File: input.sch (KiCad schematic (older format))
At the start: 64 parts, among them U301 NE5532, U302 NE5532, U303 NE5532, U304 NE5532

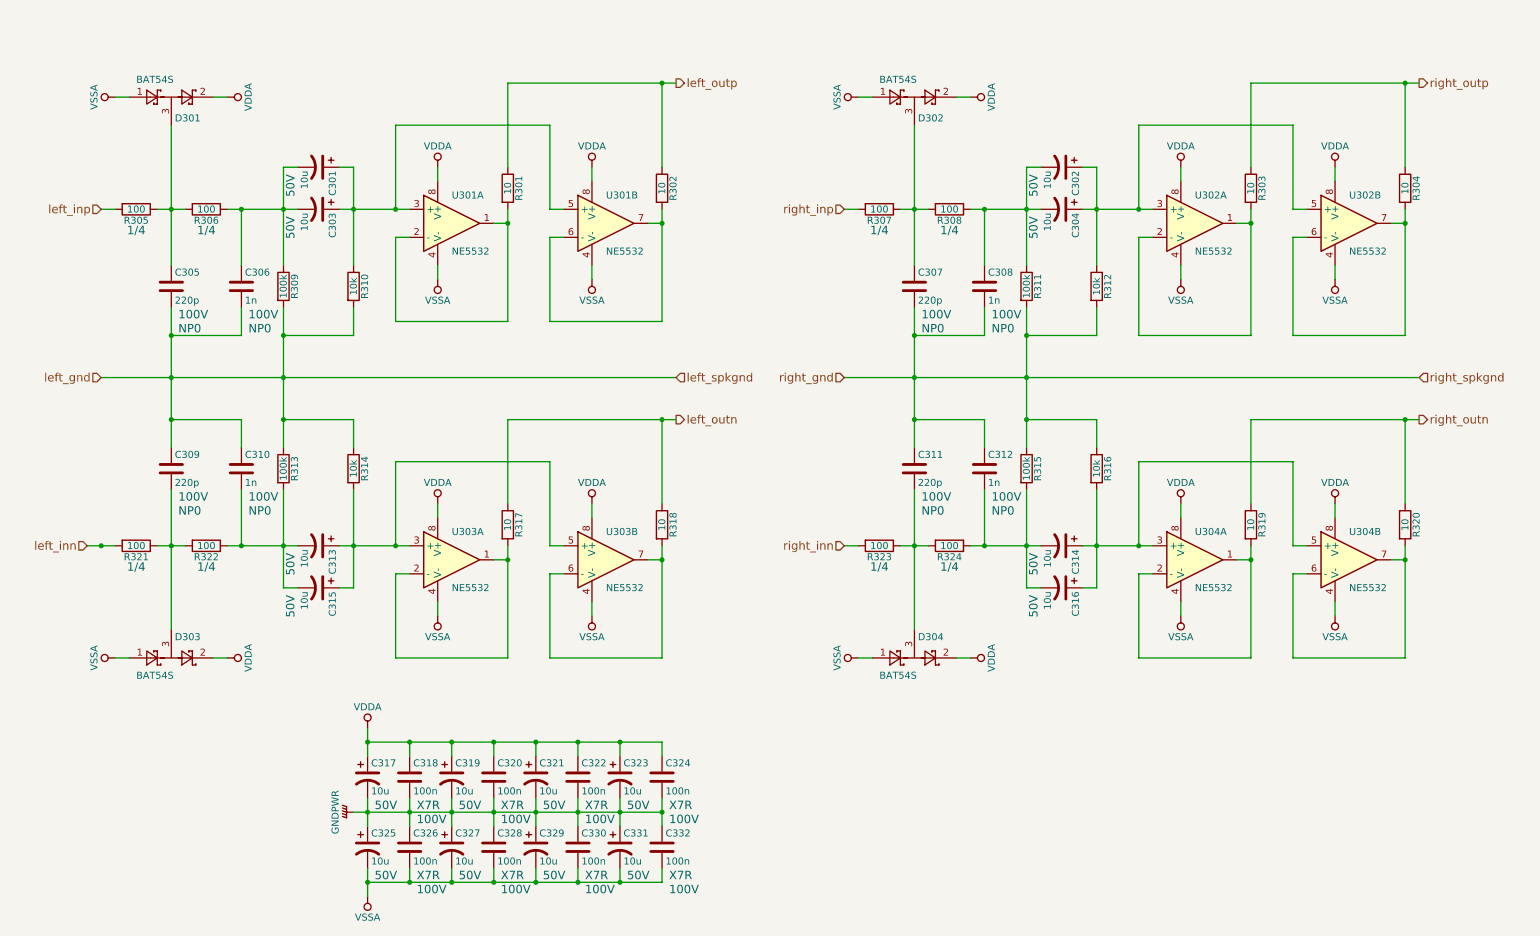
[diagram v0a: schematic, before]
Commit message: The board shall now support single channel only.
Signed-off-by: Nenad Radulovic <nenad.radulovic@seavus.com>
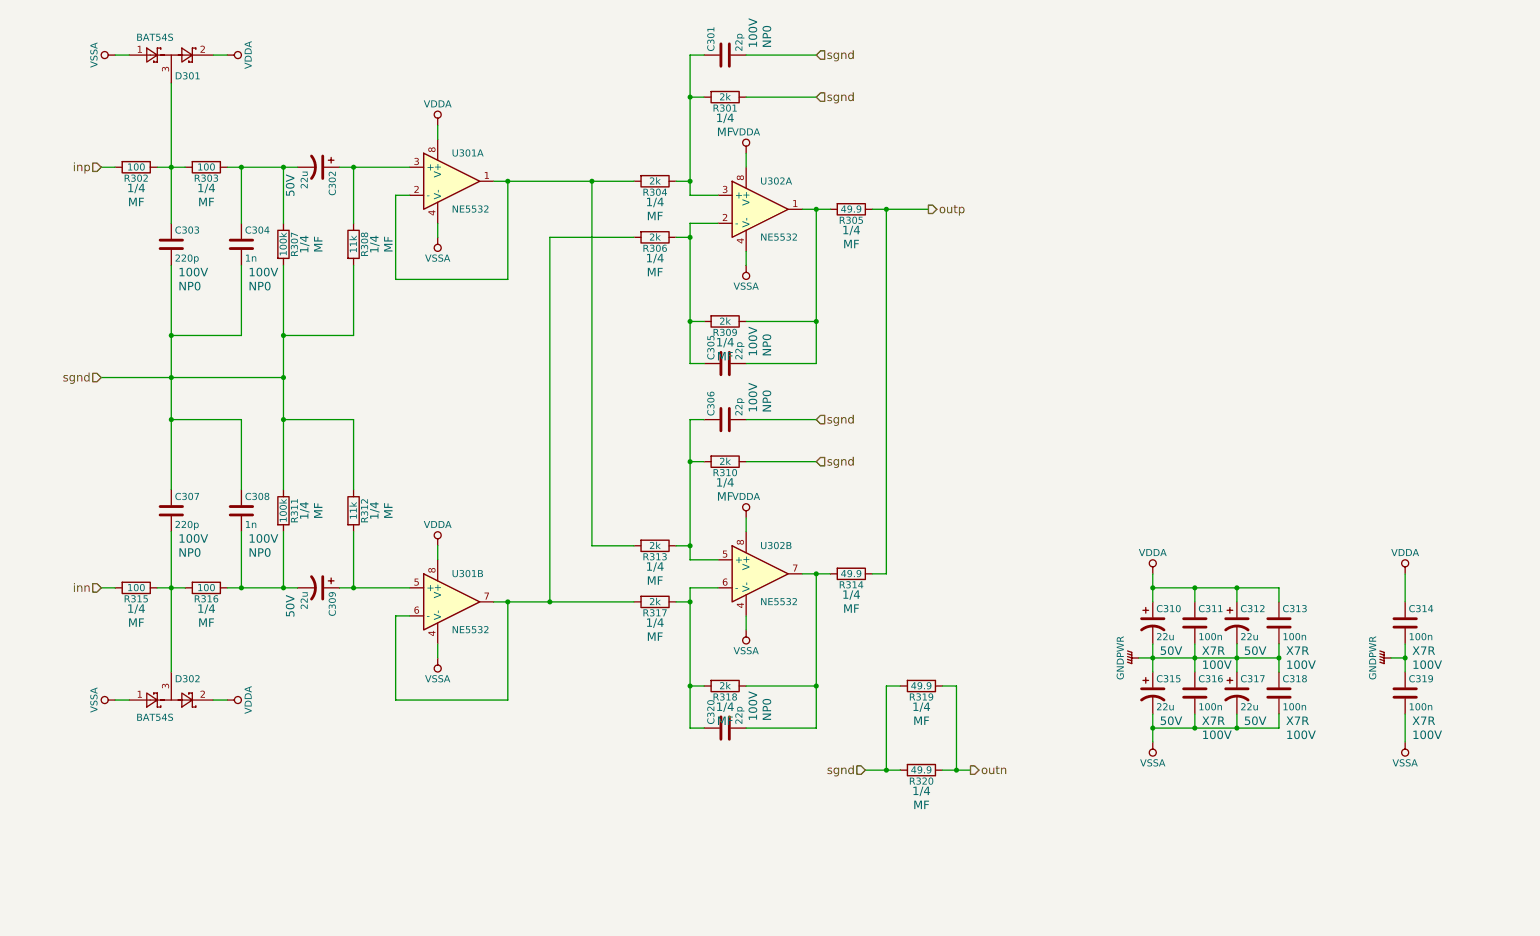
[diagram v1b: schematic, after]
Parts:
- removed C301, C302, C304, C314, C315, C316, C321, C323, C329, C331: 10u, Capacitor_THT:CP_Radial_D5.0mm_P2.00mm, symbol CP1
- removed C307, C311: 220p, Capacitor_SMD:C_0805_2012Metric_Pad1.15x1.50mm_HandSolder, symbol C
- removed C308, C312: 1n, Capacitor_SMD:C_0805_2012Metric_Pad1.15x1.50mm_HandSolder, symbol C
- removed C322, C324, C330, C332: 100n, Capacitor_SMD:C_1206_3216Metric_Pad1.24x1.80mm_HandSolder, symbol C
- removed D302, D304: BAT54S, Package_TO_SOT_SMD:SOT-23_Handsoldering, symbol BAT54S
- removed R321, R322, R323, R324: 100, Resistor_SMD:R_1206_3216Metric, symbol R
- removed unit 1 of U302
- removed unit 2 of U303
- removed U304: NE5532, Housings_DIP:DIP-8_W7.62mm_LongPads, symbol NE5532
- added C301, C305, C306, C320: 22p, Capacitor_SMD:C_0805_2012Metric_Pad1.15x1.50mm_HandSolder, symbol C
- added C314, C319: 100n, Capacitor_SMD:C_1206_3216Metric_Pad1.24x1.80mm_HandSolder, symbol C
- C302: renamed from C303; value 10u -> 22u; Manufacturer Rybicon:50YXF10MEFC5X11 -> Rybicon:50YXJ22MTA5X11; Vendor Farnell:1144632 -> Farnell:2346268
- C309: renamed from C313; value 10u -> 22u; Manufacturer Rybicon:50YXF10MEFC5X11 -> Rybicon:50YXJ22MTA5X11; Vendor Farnell:1144632 -> Farnell:2346268
- C310: renamed from C317; value 10u -> 22u; Manufacturer Rybicon:50YXF10MEFC5X11 -> Rybicon:50YXJ22MTA5X11; Vendor Farnell:1144632 -> Farnell:2346268
- C312: renamed from C319; value 10u -> 22u; Manufacturer Rybicon:50YXF10MEFC5X11 -> Rybicon:50YXJ22MTA5X11; Vendor Farnell:1144632 -> Farnell:2346268
- C315: renamed from C325; value 10u -> 22u; Manufacturer Rybicon:50YXF10MEFC5X11 -> Rybicon:50YXJ22MTA5X11; Vendor Farnell:1144632 -> Farnell:2346268
- C317: renamed from C327; value 10u -> 22u; Manufacturer Rybicon:50YXF10MEFC5X11 -> Rybicon:50YXJ22MTA5X11; Vendor Farnell:1144632 -> Farnell:2346268
- R301, R304, R317, R318: value 10 -> 2k; footprint Resistor_SMD:R_1206_3216Metric -> Resistor_SMD:R_1206_3216Metric_Pad1.24x1.80mm_HandSolder; Manufacturer (none) -> PANASONIC:ERA8ARB202V; Power (none) -> 1/4; Type (none) -> MF; Vendor (none) -> Farnell:2484813
- R302, R303: value 10 -> 100; footprint Resistor_SMD:R_1206_3216Metric -> Resistor_SMD:R_1206_3216Metric_Pad1.24x1.80mm_HandSolder; Manufacturer (none) -> PANASONIC:ERA8AEB101V; Power (none) -> 1/4; Type (none) -> MF; Vendor (none) -> Farnell:1717738
- R305: value 100 -> 49.9; footprint Resistor_SMD:R_1206_3216Metric -> Resistor_SMD:R_1206_3216Metric_Pad1.24x1.80mm_HandSolder; Manufacturer (none) -> PANASONIC:ERA8AEB49R9V; Type (none) -> MF; Vendor (none) -> Farnell:2095158
- R306: value 100 -> 2k; footprint Resistor_SMD:R_1206_3216Metric -> Resistor_SMD:R_1206_3216Metric_Pad1.24x1.80mm_HandSolder; Manufacturer (none) -> PANASONIC:ERA8ARB202V; Type (none) -> MF; Vendor (none) -> Farnell:2484813
- R307: value 100 -> 100k; footprint Resistor_SMD:R_1206_3216Metric -> Resistor_SMD:R_1206_3216Metric_Pad1.24x1.80mm_HandSolder; Manufacturer (none) -> PANASONIC:ERA8AEB104V; Type (none) -> MF; Vendor (none) -> Farnell:1717758
- R308: value 100 -> 11k; footprint Resistor_SMD:R_1206_3216Metric -> Resistor_SMD:R_1206_3216Metric_Pad1.24x1.80mm_HandSolder; Manufacturer (none) -> PANASONIC:ERA8ARB113V; Type (none) -> MF; Vendor (none) -> Farnell:2484802
- R309, R313: value 100k -> 2k; footprint Resistor_SMD:R_1206_3216Metric -> Resistor_SMD:R_1206_3216Metric_Pad1.24x1.80mm_HandSolder; Manufacturer (none) -> PANASONIC:ERA8ARB202V; Power (none) -> 1/4; Type (none) -> MF; Vendor (none) -> Farnell:2484813
- R310: value 10k -> 2k; footprint Resistor_SMD:R_1206_3216Metric -> Resistor_SMD:R_1206_3216Metric_Pad1.24x1.80mm_HandSolder; Manufacturer (none) -> PANASONIC:ERA8ARB202V; Power (none) -> 1/4; Type (none) -> MF; Vendor (none) -> Farnell:2484813
- R311: footprint Resistor_SMD:R_1206_3216Metric -> Resistor_SMD:R_1206_3216Metric_Pad1.24x1.80mm_HandSolder; Manufacturer (none) -> PANASONIC:ERA8AEB104V; Power (none) -> 1/4; Type (none) -> MF; Vendor (none) -> Farnell:1717758
- R312: value 10k -> 11k; footprint Resistor_SMD:R_1206_3216Metric -> Resistor_SMD:R_1206_3216Metric_Pad1.24x1.80mm_HandSolder; Manufacturer (none) -> PANASONIC:ERA8ARB113V; Power (none) -> 1/4; Type (none) -> MF; Vendor (none) -> Farnell:2484802
- R314: value 10k -> 49.9; footprint Resistor_SMD:R_1206_3216Metric -> Resistor_SMD:R_1206_3216Metric_Pad1.24x1.80mm_HandSolder; Manufacturer (none) -> PANASONIC:ERA8AEB49R9V; Power (none) -> 1/4; Type (none) -> MF; Vendor (none) -> Farnell:2095158
- R315: value 100k -> 100; footprint Resistor_SMD:R_1206_3216Metric -> Resistor_SMD:R_1206_3216Metric_Pad1.24x1.80mm_HandSolder; Manufacturer (none) -> PANASONIC:ERA8AEB101V; Power (none) -> 1/4; Type (none) -> MF; Vendor (none) -> Farnell:1717738
- R316: value 10k -> 100; footprint Resistor_SMD:R_1206_3216Metric -> Resistor_SMD:R_1206_3216Metric_Pad1.24x1.80mm_HandSolder; Manufacturer (none) -> PANASONIC:ERA8AEB101V; Power (none) -> 1/4; Type (none) -> MF; Vendor (none) -> Farnell:1717738
- R319, R320: value 10 -> 49.9; footprint Resistor_SMD:R_1206_3216Metric -> Resistor_SMD:R_1206_3216Metric_Pad1.24x1.80mm_HandSolder; Manufacturer (none) -> PANASONIC:ERA8AEB49R9V; Power (none) -> 1/4; Type (none) -> MF; Vendor (none) -> Farnell:2095158
- renumbered C305 to C303, C306 to C304, C309 to C307, C310 to C308, C318 to C311, C320 to C313, C326 to C316, C328 to C318, D303 to D302, U303 to U301, U301 to U302
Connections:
- net right_inp is gone; now on net sgnd: R307.2
- net GNDPWR: now also C314.2, C319.1
- net VDDA: now also C314.1
- net VSSA: now also C319.2
- net at U301.1, U301.2 (-): now also R304.2, R313.2; no longer R301.2
- net at C302.1, U301.3 (+): now also R308.1; no longer R310.1, U302.5 (+)
- net at C302.2, C304.1: now also R303.1, R307.1; no longer R306.1, R309.1
- net at C303.1, D301.3: now also R302.1, R303.2; no longer R305.1, R306.2
- net at R318.2: now also R317.1, U302.6 (-), C320.1
- net at C308.2, C309.2: now also R311.2, R316.1; no longer R313.2
- net at C307.2, D302.3: now also R315.1, R316.2
- net at U302.5 (+): now also R310.2, R313.1, C306.1; no longer R312.1
- net sgnd: now reaches R311.1
- net sgnd: now also C303.2, C304.2, C307.1, C308.1, R301.1, R308.2, R310.1, R312.1, R319.2, R320.2, C301.2, C306.2; no longer R308.1
- net inn: now reaches R315.2
- removed net left_gnd: C303.2, C304.2, C307.1, C308.1, R309.2, R310.2, R313.1, R314.1
- net left_inp: no longer names the net of R305.2
- net left_inp: now also R309.1, U302.1, C305.2
- net left_outn: no longer names the net of R318.1
- net left_outn: now also R314.2, U302.7, C320.2; no longer R317.1
- removed net left_outp: R301.1, R302.1
- removed net right_gnd: R311.2, R312.2, R315.1, R316.1
- net right_outn renamed outn
- net right_outp: no longer names the net of R304.1
- net right_outp: now also R301.2, U302.3 (+), C301.1; no longer R303.1
- new net: C305.1, R306.1, R309.2, U302.2 (-)
- new net: C309.1, R312.2, U301.5 (+)
- new net: R306.2, R317.2, U301.6 (-), U301.7
- new net inp: R302.2
- new net outp: R305.1, R314.1
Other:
- moved on the sheet: C302, C303, C304, C307, C308, C309, C310, C311, C312, C313, C315, C316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

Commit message: Switched to Kicad 5.0
Signed-off-by: Nenad Radulovic <nenad.b.radulovic@gmail.com>
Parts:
- removed C301, C305, C306, C320: 22p, Capacitor_SMD:C_0805_2012Metric_Pad1.15x1.50mm_HandSolder, symbol C
- removed C302, C309, C310, C312, C315, C317: 22u, Capacitor_THT:CP_Radial_D5.0mm_P2.00mm, symbol CP1
- removed C307: 220p, Capacitor_SMD:C_0805_2012Metric_Pad1.15x1.50mm_HandSolder, symbol C
- removed C308: 1n, Capacitor_SMD:C_0805_2012Metric_Pad1.15x1.50mm_HandSolder, symbol C
- removed C311, C313, C314, C316, C318, C319: 100n, Capacitor_SMD:C_1206_3216Metric_Pad1.24x1.80mm_HandSolder, symbol C
- removed D301, D302: BAT54S, Package_TO_SOT_SMD:SOT-23_Handsoldering, symbol BAT54S
- removed R301, R304, R306, R309, R310, R313, R317, R318: 2k, Resistor_SMD:R_1206_3216Metric_Pad1.24x1.80mm_HandSolder, symbol R
- removed R305, R314, R319, R320: 49.9, Resistor_SMD:R_1206_3216Metric_Pad1.24x1.80mm_HandSolder, symbol R
- removed R308, R312: 11k, Resistor_SMD:R_1206_3216Metric_Pad1.24x1.80mm_HandSolder, symbol R
- removed R311: 100k, Resistor_SMD:R_1206_3216Metric_Pad1.24x1.80mm_HandSolder, symbol R
- removed R315, R316: 100, Resistor_SMD:R_1206_3216Metric_Pad1.24x1.80mm_HandSolder, symbol R
- removed U301, U302: NE5532, Housings_DIP:DIP-8_W7.62mm_LongPads, symbol NE5532
- added R12: 10, Resistor_THT:R_Axial_DIN0309_L9.0mm_D3.2mm_P12.70mm_Horizontal, symbol Device:R
- C12: renamed from C303; footprint Capacitor_SMD:C_0805_2012Metric_Pad1.15x1.50mm_HandSolder -> Capacitor_THT:C_Disc_D4.3mm_W1.9mm_P5.00mm; symbol C -> Device:C
- C13: renamed from C304; footprint Capacitor_SMD:C_0805_2012Metric_Pad1.15x1.50mm_HandSolder -> Capacitor_THT:C_Disc_D4.3mm_W1.9mm_P5.00mm; symbol C -> Device:C
- R10: renamed from R303; footprint Resistor_SMD:R_1206_3216Metric_Pad1.24x1.80mm_HandSolder -> Resistor_THT:R_Axial_DIN0207_L6.3mm_D2.5mm_P10.16mm_Horizontal; symbol R -> Device:R
- R11: renamed from R307; footprint Resistor_SMD:R_1206_3216Metric_Pad1.24x1.80mm_HandSolder -> Resistor_THT:R_Axial_DIN0207_L6.3mm_D2.5mm_P10.16mm_Horizontal; symbol R -> Device:R
- R9: renamed from R302; footprint Resistor_SMD:R_1206_3216Metric_Pad1.24x1.80mm_HandSolder -> Resistor_THT:R_Axial_DIN0207_L6.3mm_D2.5mm_P10.16mm_Horizontal; symbol R -> Device:R
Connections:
- net GNDPWR: now also R12.1
- net outp: now also C13.1, R10.1, R11.1
- net sgnd: now also R12.2
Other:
- moved on the sheet: R11

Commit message: Release Version 1.0
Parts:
- C12: Manufacturer Multicomp:MCMT21N221F101CT -> AVX:SR211A221JAR; Vendor Farnell:1856271 -> Farnell:1100508
- C13: Manufacturer Multicomp:MCMT21N102F101CT -> AVX:SR211A102KAR; Vendor Farnell:1856276 -> Farnell:1100513
- R10, R9: Manufacturer PANASONIC:ERA8AEB101V -> TE Connectivity:LR0204F100R; Power 1/4 -> 0.25W; Vendor Farnell:1717738 -> Farnell:2329854
- R11: Manufacturer PANASONIC:ERA8AEB104V -> TE Connectivity:LR0204F100K; Power 1/4 -> 0.25W; Vendor Farnell:1717758 -> Farnell:2329853
- R12: footprint Resistor_THT:R_Axial_DIN0309_L9.0mm_D3.2mm_P12.70mm_Horizontal -> Resistor_THT:R_Axial_DIN0207_L6.3mm_D2.5mm_P10.16mm_Horizontal; Manufacturer NEOHM-TE:FRN50J10R/S -> TE Connectivity:LR1F10R; Power 1/4 -> 0.6W; Type MO -> MF; Vendor Farnell:1898502 -> Farnell:2329993
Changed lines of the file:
@@
 F 1 "1n" H 2125 2450 50  0000 L CNN
 F 2 "Capacitor_THT:C_Disc_D4.3mm_W1.9mm_P5.00mm" H 2138 2400 50  0001 C CNN
-F 3 "http://www.farnell.com/datasheets/1825496.pdf" H 2100 2550 50  0001 C CNN
+F 3 "http://www.farnell.com/datasheets/2095938.pdf" H 2100 2550 50  0001 C CNN
 F 4 "100V" H 2150 2350 60  0000 L CNN "Voltage"
 F 5 "NP0" H 2150 2250 60  0000 L CNN "Type"
-F 6 "Farnell:1856276" H 2100 2550 60  0001 C CNN "Vendor"
-F 7 "Multicomp:MCMT21N102F101CT" H 2100 2550 60  0001 C CNN "Manufacturer"
+F 6 "Farnell:1100513" H 2100 2550 60  0001 C CNN "Vendor"
+F 7 "AVX:SR211A102KAR" H 2100 2550 60  0001 C CNN "Manufacturer"
 	1    2100 2550
 	1    0    0    -1
@@
 F 1 "220p" H 1625 2450 50  0000 L CNN
 F 2 "Capacitor_THT:C_Disc_D4.3mm_W1.9mm_P5.00mm" H 1638 2400 50  0001 C CNN
-F 3 "http://www.farnell.com/datasheets/1825496.pdf" H 1600 2550 50  0001 C CNN
+F 3 "http://www.farnell.com/datasheets/2095938.pdf" H 1600 2550 50  0001 C CNN
 F 4 "100V" H 1650 2350 60  0000 L CNN "Voltage"
 F 5 "NP0" H 1650 2250 60  0000 L CNN "Type"
-F 6 "Farnell:1856271" H 1600 2550 60  0001 C CNN "Vendor"
-F 7 "Multicomp:MCMT21N221F101CT" H 1600 2550 60  0001 C CNN "Manufacturer"
+F 6 "Farnell:1100508" H 1600 2550 60  0001 C CNN "Vendor"
+F 7 "AVX:SR211A221JAR" H 1600 2550 60  0001 C CNN "Manufacturer"
 	1    1600 2550
 	1    0    0    -1
@@
 F 1 "100" V 1350 2000 50  0000 C CNN
 F 2 "Resistor_THT:R_Axial_DIN0207_L6.3mm_D2.5mm_P10.16mm_Horizontal" V 1280 2000 50  0001 C CNN
-F 3 "http://www.farnell.com/datasheets/2052875.pdf" H 1350 2000 50  0001 C CNN
-F 4 "Farnell:1717738" V 1350 2000 60  0001 C CNN "Vendor"
-F 5 "PANASONIC:ERA8AEB101V" V 1350 2000 60  0001 C CNN "Manufacturer"
+F 3 "http://www.farnell.com/datasheets/1723855.pdf" H 1350 2000 50  0001 C CNN
+F 4 "Farnell:2329854" V 1350 2000 60  0001 C CNN "Vendor"
+F 5 "TE Connectivity:LR0204F100R" V 1350 2000 60  0001 C CNN "Manufacturer"
 F 6 "MF" V 1600 2000 60  0000 C CNN "Type"
-F 7 "1/4" V 1500 2000 60  0000 C CNN "Power"
+F 7 "0.25W" V 1500 2000 60  0000 C CNN "Power"
 	1    1350 2000
 	0    1    1    0
@@
 F 1 "100" V 1850 2000 50  0000 C CNN
 F 2 "Resistor_THT:R_Axial_DIN0207_L6.3mm_D2.5mm_P10.16mm_Horizontal" V 1780 2000 50  0001 C CNN
-F 3 "http://www.farnell.com/datasheets/2052875.pdf" H 1850 2000 50  0001 C CNN
-F 4 "Farnell:1717738" V 1850 2000 60  0001 C CNN "Vendor"
-F 5 "PANASONIC:ERA8AEB101V" V 1850 2000 60  0001 C CNN "Manufacturer"
+F 3 "http://www.farnell.com/datasheets/1723855.pdf" H 1850 2000 50  0001 C CNN
+F 4 "Farnell:2329854" V 1850 2000 60  0001 C CNN "Vendor"
+F 5 "TE Connectivity:LR0204F100R" V 1850 2000 60  0001 C CNN "Manufacturer"
 F 6 "MF" V 2100 2000 60  0000 C CNN "Type"
-F 7 "1/4" V 2000 2000 60  0000 C CNN "Power"
+F 7 "0.25W" V 2000 2000 60  0000 C CNN "Power"
 	1    1850 2000
 	0    1    1    0
@@
 F 0 "R12" V 3430 3200 50  0000 C CNN
 F 1 "10" V 3350 3200 50  0000 C CNN
-F 2 "Resistor_THT:R_Axial_DIN0309_L9.0mm_D3.2mm_P12.70mm_Horizontal" V 3280 3200 50  0001 C CNN
-F 3 "http://www.farnell.com/datasheets/1332875.pdf?_ga=2.142443770.970921211.1525990156-997268051.1515705412" H 3350 3200 50  0001 C CNN
-F 4 "MO" V 3600 3200 60  0000 C CNN "Type"
-F 5 "1/4" V 3500 3200 60  0000 C CNN "Power"
-F 6 "Farnell:1898502" V 3350 3200 60  0001 C CNN "Vendor"
-F 7 "NEOHM-TE:FRN50J10R/S" V 3350 3200 60  0001 C CNN "Manufacturer"
+F 2 "Resistor_THT:R_Axial_DIN0207_L6.3mm_D2.5mm_P10.16mm_Horizontal" V 3280 3200 50  0001 C CNN
+F 3 "http://www.farnell.com/datasheets/1723855.pdf" H 3350 3200 50  0001 C CNN
+F 4 "Farnell:2329993" V 3350 3200 60  0001 C CNN "Vendor"
+F 5 "TE Connectivity:LR1F10R" V 3350 3200 60  0001 C CNN "Manufacturer"
+F 6 "0.6W" V 3500 3200 60  0000 C CNN "Power"
+F 7 "MF" V 3600 3200 60  0000 C CNN "Type"
 	1    3350 3200
 	0    1    1    0
@@
 F 1 "100k" V 2600 2550 50  0000 C CNN
 F 2 "Resistor_THT:R_Axial_DIN0207_L6.3mm_D2.5mm_P10.16mm_Horizontal" V 2530 2550 50  0001 C CNN
-F 3 "http://www.farnell.com/datasheets/2052875.pdf" H 2600 2550 50  0001 C CNN
-F 4 "Farnell:1717758" V 2600 2550 60  0001 C CNN "Vendor"
-F 5 "PANASONIC:ERA8AEB104V" V 2600 2550 60  0001 C CNN "Manufacturer"
+F 3 "http://www.farnell.com/datasheets/1723855.pdf" H 2600 2550 50  0001 C CNN
+F 4 "Farnell:2329853" V 2600 2550 60  0001 C CNN "Vendor"
+F 5 "TE Connectivity:LR0204F100K" V 2600 2550 60  0001 C CNN "Manufacturer"
 F 6 "MF" V 2850 2550 60  0000 C CNN "Type"
-F 7 "1/4" V 2750 2550 60  0000 C CNN "Power"
+F 7 "0.25W" V 2750 2550 60  0000 C CNN "Power"
 	1    2600 2550
 	1    0    0    -1
